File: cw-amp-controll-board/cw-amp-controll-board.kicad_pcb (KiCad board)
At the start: 4 copper layers, 80 x 100 mm, 64 parts, among them J1 Conn_02x07_Odd_Even, J2 Conn_01x06, J3 Conn_02x05_Odd_Even, J4 Conn_01x03_Male, Q1 BC850, Q2 BC850, Q3 BC850, Q4 BC850, SW1 RotaryEncoder, U1 LDL1117S33R, U2 PCF8574, U3 ESP32-C3-WROOM-02, U4 AT42QT2120-CommsMode, U5 PCF8574, U6 PCM5100A

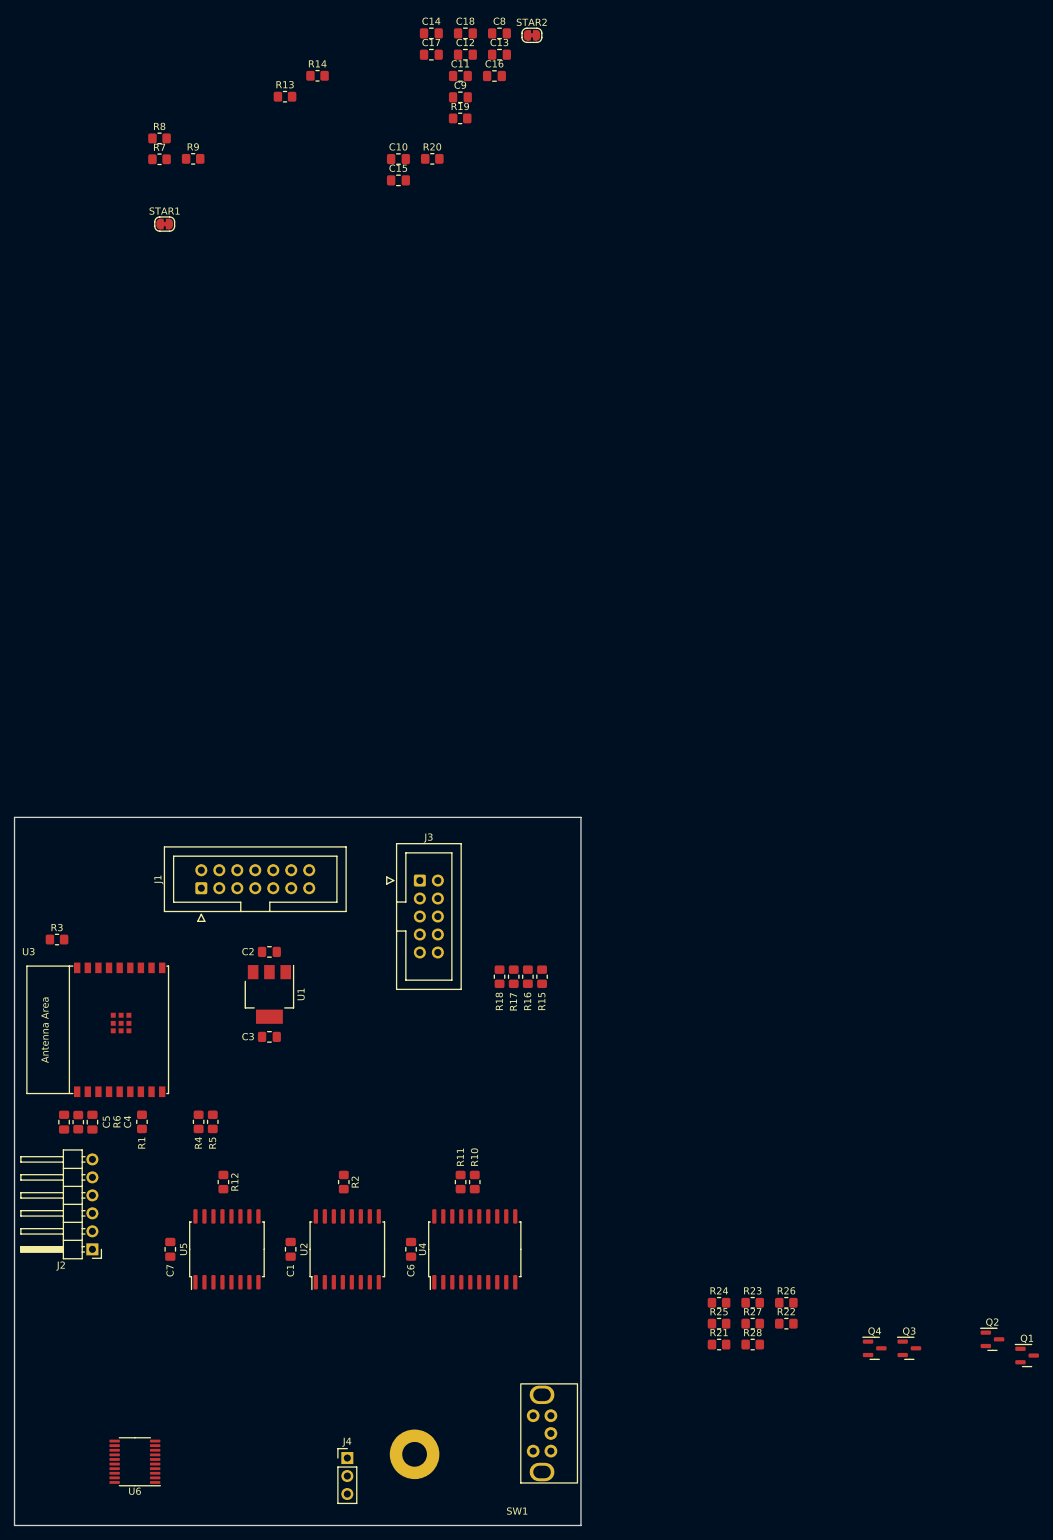
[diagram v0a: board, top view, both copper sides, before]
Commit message: First placement controll board
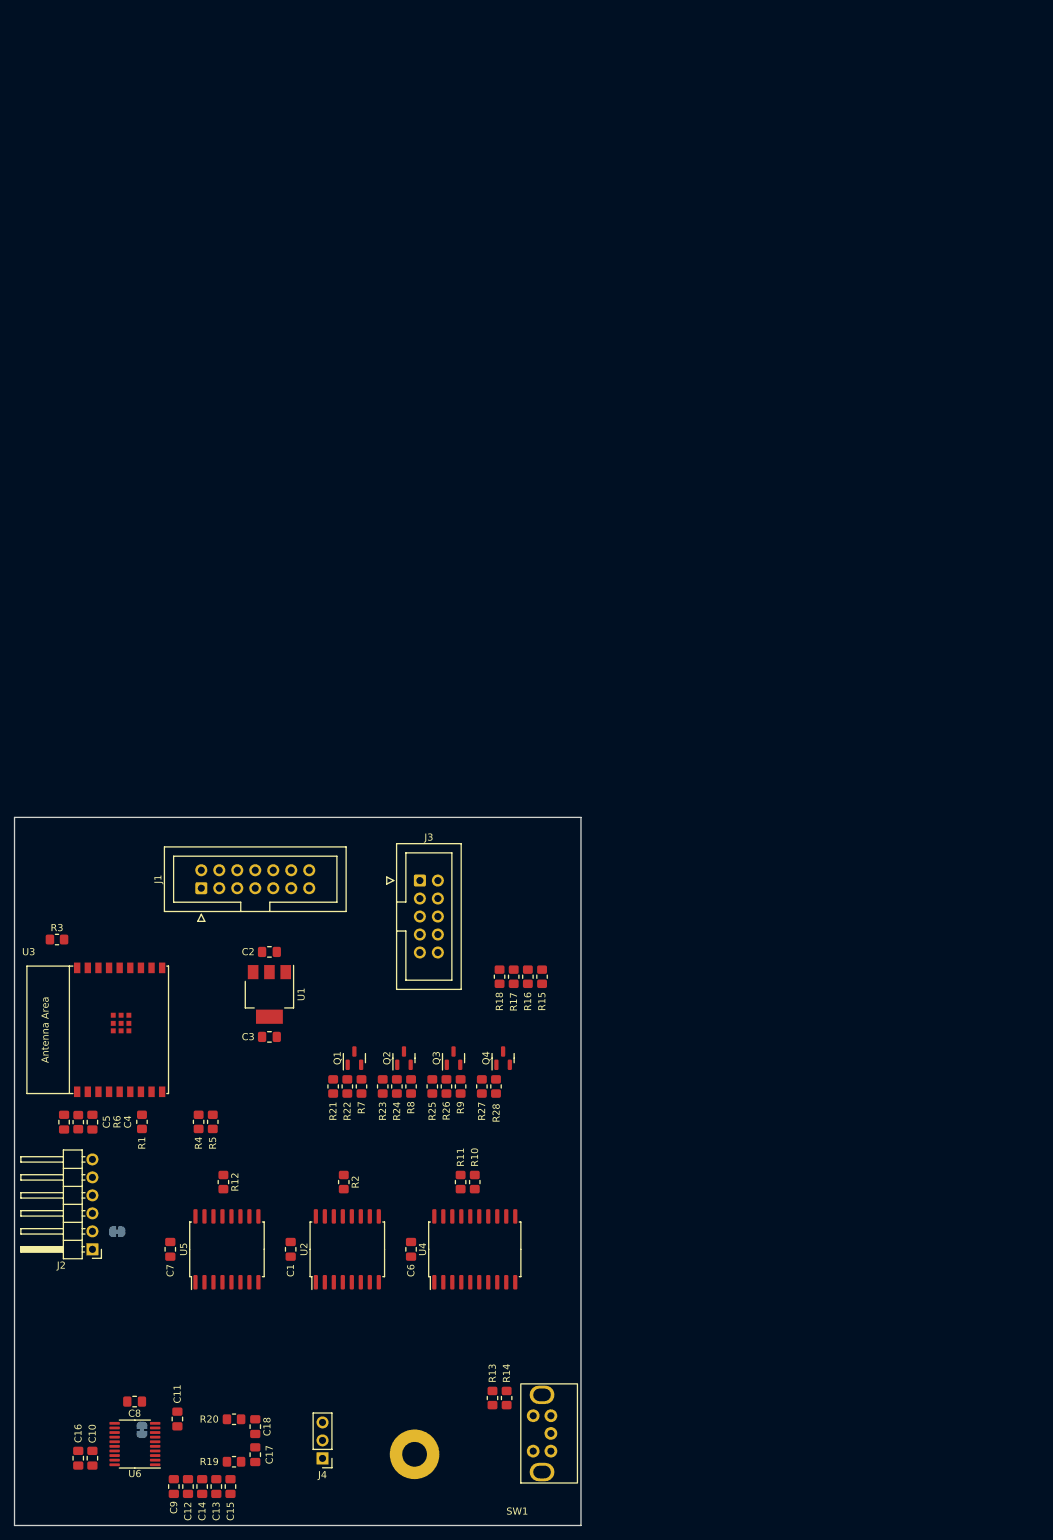
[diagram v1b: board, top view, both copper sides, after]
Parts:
- STAR1, STAR2: moved to B.Cu
- moved C14 207.8 mm to (136.5, 152.5), turned to 90 degrees
- moved C13 206.1 mm to (138.5, 152.5), turned to 90 degrees
- moved C12 206.0 mm to (134.5, 152.5), turned to 90 degrees
- moved STAR2 204.5 mm to (128.0, 144.5), turned to -90 degrees
- moved C16 203.9 mm to (119.0, 148.5), turned to 90 degrees
- moved C9 200.3 mm to (132.5, 152.5), turned to 90 degrees
- moved C8 200.0 mm to (127.0, 140.5), turned to 180 degrees
- moved C17 199.3 mm to (144.0, 148.0), turned to 90 degrees
- moved C18 199.0 mm to (144.0, 144.0), turned to -90 degrees
- moved C11 193.8 mm to (133.0, 143.0), turned to 90 degrees
- moved R19 192.4 mm to (141.0, 149.0)
- moved R14 188.6 mm to (179.5, 140.0), turned to -90 degrees
- moved C10 188.5 mm to (121.0, 148.5), turned to 90 degrees
- moved R13 186.1 mm to (177.5, 140.0), turned to -90 degrees
- moved C15 186.0 mm to (140.5, 152.5), turned to 90 degrees
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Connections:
- J2 pad 6: GND -> GNDD
- SW1 pad C: GND -> GNDD

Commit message: Placement 2 controll board
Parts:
- moved REF** 10.6 mm to (155.9, 147.0), turned to 180 degrees
- moved R3 6.00 mm to (122.0, 75.2), turned to -90 degrees
- moved J4 5.00 mm to (148.5, 148.5)
- moved J3 2.49 mm to (165.0, 68.0), turned to 90 degrees
- moved C10 1.50 mm to (119.5, 148.5)
- moved C11 1.50 mm to (131.5, 142.9)
- moved C12 1.50 mm to (133.0, 152.5)
- moved C13 1.50 mm to (137.0, 152.5)
- moved C14 1.50 mm to (135.0, 152.5)
- moved C15 1.50 mm to (139.0, 152.5)
- moved C16 1.50 mm to (117.5, 148.5)
- moved C17 1.50 mm to (142.5, 148.0)
- moved C18 1.50 mm to (142.5, 144.0)
- moved C8 1.50 mm to (125.5, 140.5)
- moved C9 1.50 mm to (131.0, 152.5)
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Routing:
- net GNDD: track 0.00 -> 311.5 mm, vias 0 -> 10
- net +3V3: track 0.00 -> 205.3 mm, vias 0 -> 8
- net +5V: track 0.00 -> 18.7 mm, vias 0 -> 1
- net GNDA: track 0.00 -> 11.4 mm, vias 0 -> 1
- net /ESP-AUDIO/LDOO: track 0.00 -> 5.72 mm
- net /GPIO2: track 0.00 -> 3.06 mm
- net /0: track 0.00 -> 2.87 mm
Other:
- board size 80 x 100 mm -> 78 x 100 mm

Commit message: routing controller
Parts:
- added FID1: Fiducial, Fiducial:Fiducial_1.5mm_Mask3mm, F.Cu at (117.0, 63.0)
- added FID2: Fiducial, Fiducial:Fiducial_1.5mm_Mask3mm, F.Cu at (117.0, 153.0)
- added FID3: Fiducial, Fiducial:Fiducial_1.5mm_Mask3mm, F.Cu at (187.5, 63.0)
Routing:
- net +3V3: track 205.3 -> 471.7 mm, vias 8 -> 17
- net GNDD: track 311.5 -> 523.1 mm, vias 10 -> 16
- net SCL: track 0.00 -> 143.6 mm, vias 0 -> 6
- net SDA: track 0.00 -> 140.2 mm, vias 0 -> 5
- net AMP-GAIN1: track 0.00 -> 111.5 mm, vias 0 -> 2
- net AMP-GAIN0: track 0.00 -> 105.1 mm, vias 0 -> 2
- net GPIO6: track 0.00 -> 103.5 mm, vias 0 -> 2
- net GPIO7: track 0.00 -> 102.7 mm, vias 0 -> 2
- net AMP-ShutDown: track 0.00 -> 98.1 mm, vias 0 -> 2
- net ~{AMP-Mute}: track 0.00 -> 88.5 mm, vias 0 -> 2
- net DIN: track 0.00 -> 83.9 mm, vias 0 -> 2
- net LRCLK: track 0.00 -> 82.6 mm, vias 0 -> 2
- net BCK: track 0.00 -> 81.6 mm, vias 0 -> 2
- net BT-KEY: track 0.00 -> 80.2 mm, vias 0 -> 2
- net LED-BT: track 0.00 -> 78.9 mm, vias 0 -> 2
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- added copper zone on F.Cu, net +3V3
- added copper zone on In2.Cu, net +3V3
- added copper zone on In2.Cu, net +5V
- added copper zone on B.Cu, net GNDA
- added copper zone on F.Cu, net GNDA
- added copper zone on In1.Cu, net GNDA
- added copper zone on B.Cu, net GNDD
- added copper zone on F.Cu, net GNDD
- added copper zone on In1.Cu, net GNDD
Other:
- board text added: "0 / IO9"
- board text added: "3V3"
- board text added: "42Volt.de"
- board text added: "AMP-Connector"
- board text added: "C@mpuswoche"
- board text added: "CW-AMP-Controll V1.0 Lars Nienhaus"
- board text added: "FP-Connector"
- board text added: "GND"
- board text added: "L"
- board text added: "L1"
- board text added: "L2"
- board text added: "L3"
- board text added: "L4"
- board text added: "R"
- board text added: "RST"
- board text added: "RxD µC"
- board text added: "TxD µC"
- board text added: "Westfälische Hochschule"
- board text added: "www.campuswoche.de"

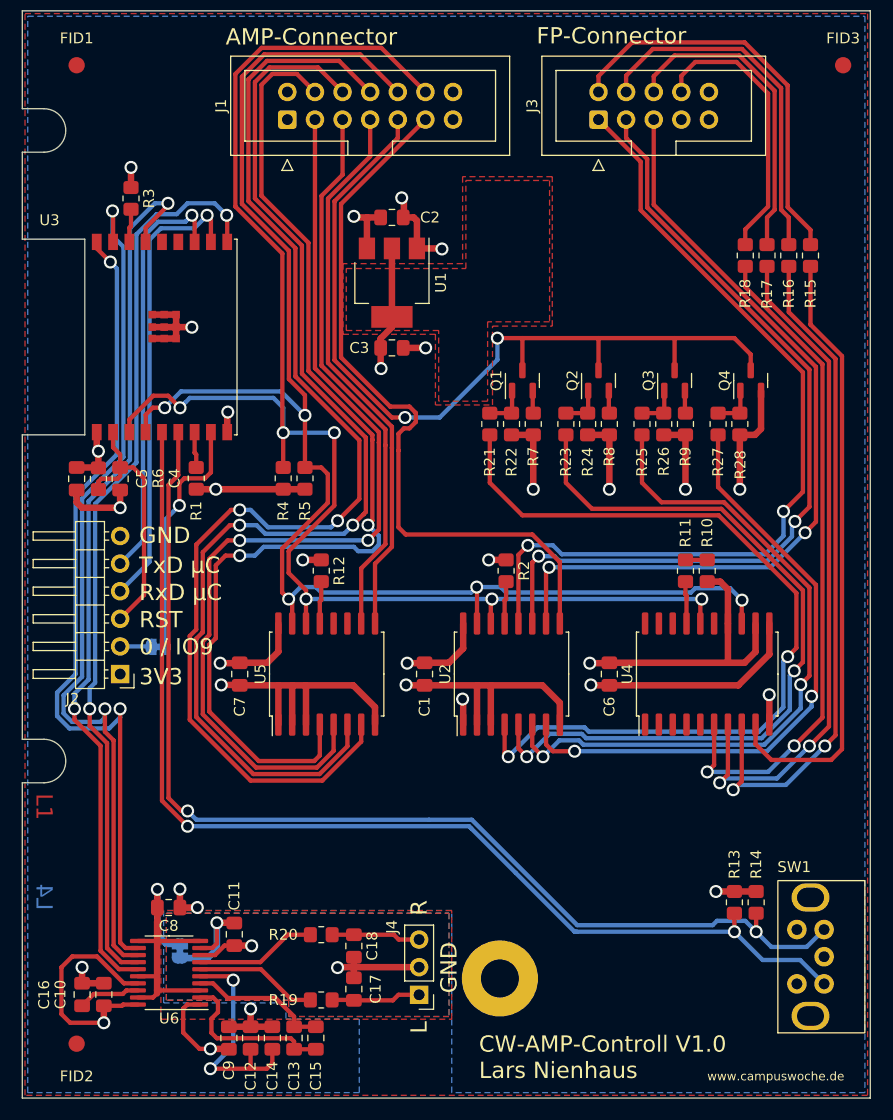
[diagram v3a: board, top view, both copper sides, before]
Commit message: removed errors control board, added interrupt pins controllboard
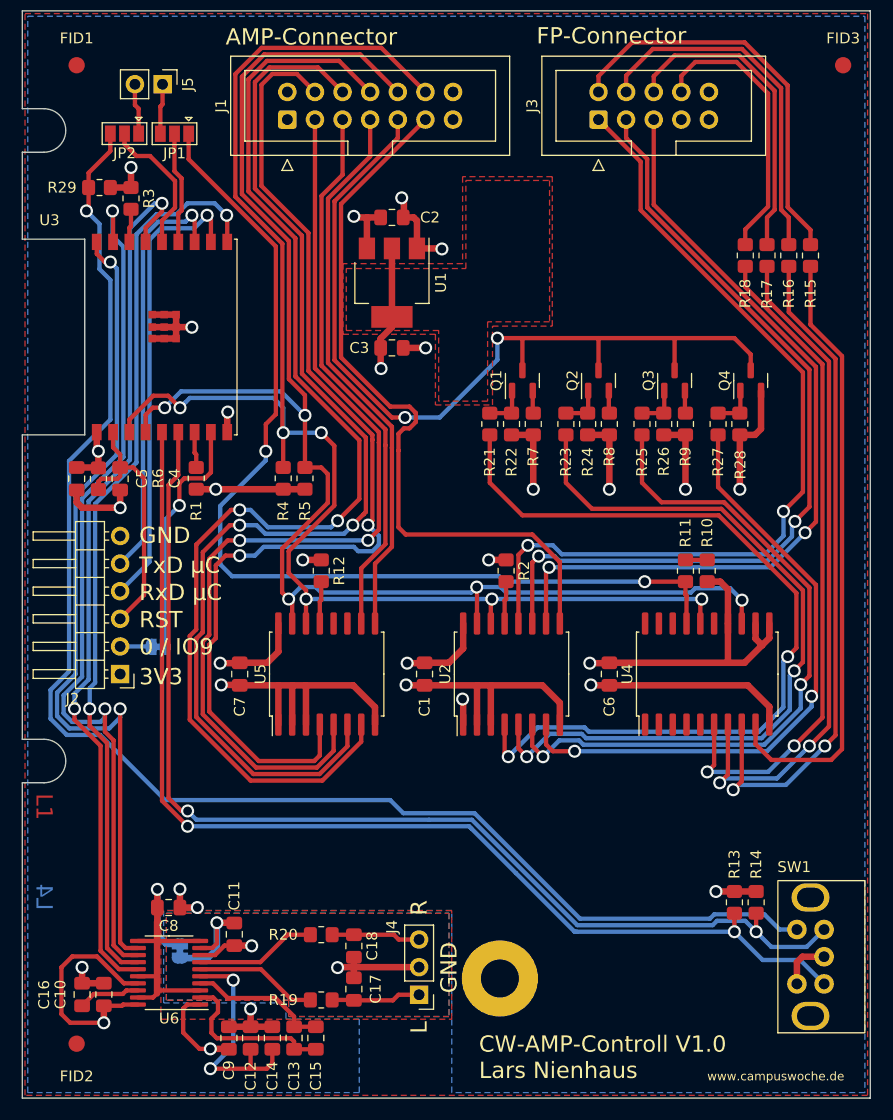
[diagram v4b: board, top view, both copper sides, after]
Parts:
- added J5: Conn_01x02, Connector_PinHeader_2.54mm:PinHeader_1x02_P2.54mm_Vertical, F.Cu at (124.9, 64.8)
- added JP1: Jumper_3_Open, Jumper:SolderJumper-3_P1.3mm_Open_Pad1.0x1.5mm, F.Cu at (126.0, 69.3)
- added JP2: Jumper_3_Open, Jumper:SolderJumper-3_P1.3mm_Open_Pad1.0x1.5mm, F.Cu at (121.4, 69.3)
- added R29: 10k, Resistor_SMD:R_0805_2012Metric_Pad1.20x1.40mm_HandSolder, F.Cu at (119.1, 74.2)
- SW1: value RotaryEncoder -> RotaryEncoder_Switch
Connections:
- U3 pad 13: unconnected-(U3-Pad13) -> Net-(U3-Pad13)
- U3 pad 14: unconnected-(U3-Pad14) -> Net-(U3-Pad14)
- U4 pad 10: +3V3 -> GNDD
- U4 pad 11: GNDD -> +3V3
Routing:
- net ROTARY-SWITCH: track 0.00 -> 134.9 mm, vias 0 -> 1
- net ~{TOUCH-INT}: track 3.89 -> 92.4 mm, vias 0 -> 2
- net +3V3: track 471.7 -> 455.9 mm, vias 17 -> 16
- net Net-(U3-Pad14): track 0.00 -> 13.1 mm
- net Net-(U3-Pad13): track 0.00 -> 10.3 mm
- net Net-(J5-Pad2): track 0.00 -> 4.68 mm
- net Net-(J5-Pad1): track 0.00 -> 4.63 mm
- net GNDD: track 523.1 -> 526.3 mm
- net LRCLK: track 82.6 -> 81.8 mm
- net SCL: track 143.6 -> 142.8 mm
